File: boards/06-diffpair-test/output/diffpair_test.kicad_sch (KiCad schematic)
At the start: 7 parts, among them J1 USB-C, J3 MiniPCIe, J4 FFC4, U1 QFN32_USB2, U2 BGA49_USB3, U3 QFP48_PCIe, U4 QFN24_MIPI

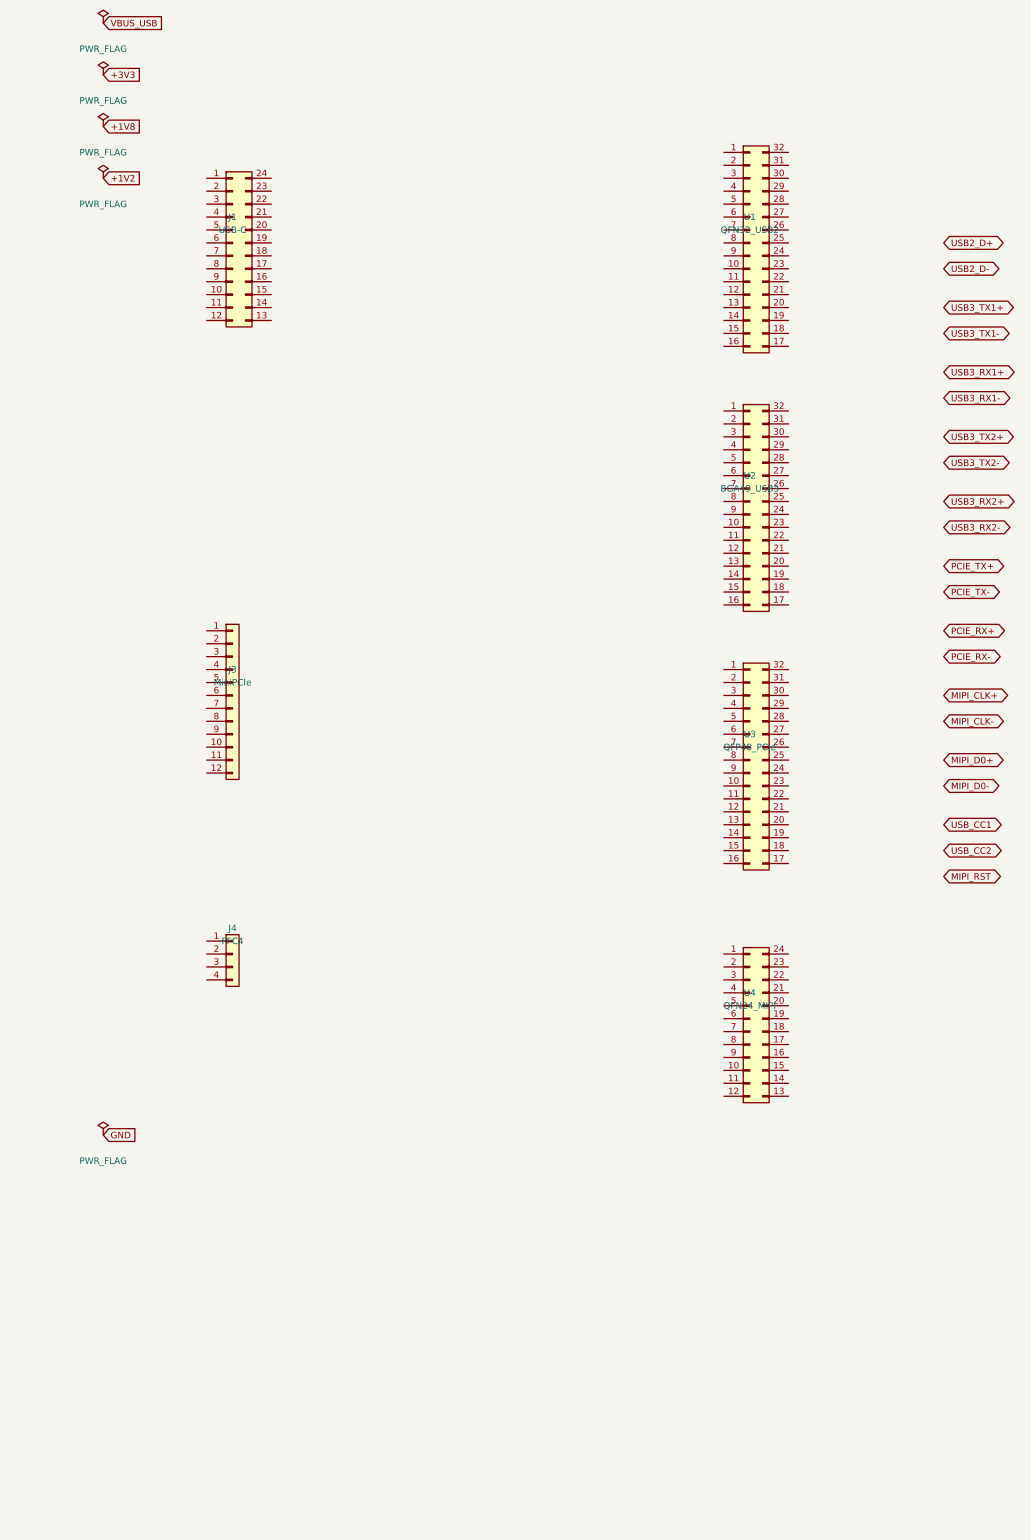
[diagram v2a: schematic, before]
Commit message: feat(lvs): wire boards 06/07 fixture schematics so LVS carries real evidence
Boards 06 (diffpair-test) and 07 (matchgroup-test) showed "LVS not run"
on the gallery because their PCB-first fixture schematics contained ZERO
(wire ...) elements: every pin floated, _schematic_pin_to_net bound 0
pins, and the #4011 vacuity guard correctly refused clean=true on zero
evidence.  This wires both schematics for real:

Schematic generators (the fix):
* Both generate_schematic.py scripts now synthesize one testbench symbol
  per component via kicad_tools.schematic.symbol_generator, with pin
  numbers matching the PCB pads EXACTLY (USB-C A1..B12+S1/S2, BGA A1..G7,
  FFC M1/M2/RST -- stock Conn_01xN symbols with numeric pins could never
  bind those pads), written to a project-local .kicad_sym and resolved
  via Schematic(local_symbol_libs=[...]) (the board-05 pattern).
* Every pin gets a wire stub (endpoint-attached, per KiCad semantics) +
  a global label naming its net; PIN_NETS mirrors generate_pcb.py
  pad-for-pad.  Bound pins: board 06 0/198 -> 198/198, board 07
  0/244 -> 244/244.

Verified LVS outcomes (committed artifacts):
* Board 06: copper 0 shorts / 0 opens on 198 bound pads AND label 0
  mismatches -> lvs.json clean=true; recipe now hard-gates on BOTH
  comparators (require_clean=True, boards 00-02 style).  board.json:
  status=ok, lvs_clean=true -> gallery Ready.
* Board 07: label clean, copper HONESTLY reports exactly the 5
  seed-invariant unroutable nets (#3438: DQ3, DQ4, MIPI_DAT0_N,
  TMDS_D0_N, TMDS_D1_N) as opens -> committed lvs.json clean=false with
  5 copper opens.  Recipe keeps require_clean=False (the opens are
  expected) with an accurate warning.  board.json: status=partial,
  lvs_clean=false, lvs_mismatches=5 -- the truthful state.

board-metrics:
* _parse_lvs now counts copper_mismatches in lvs_mismatches (label leg
  alone would render a dishonest "0 mismatches" for board 07's
  clean=false report).  All other committed boards have 0 copper
  mism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
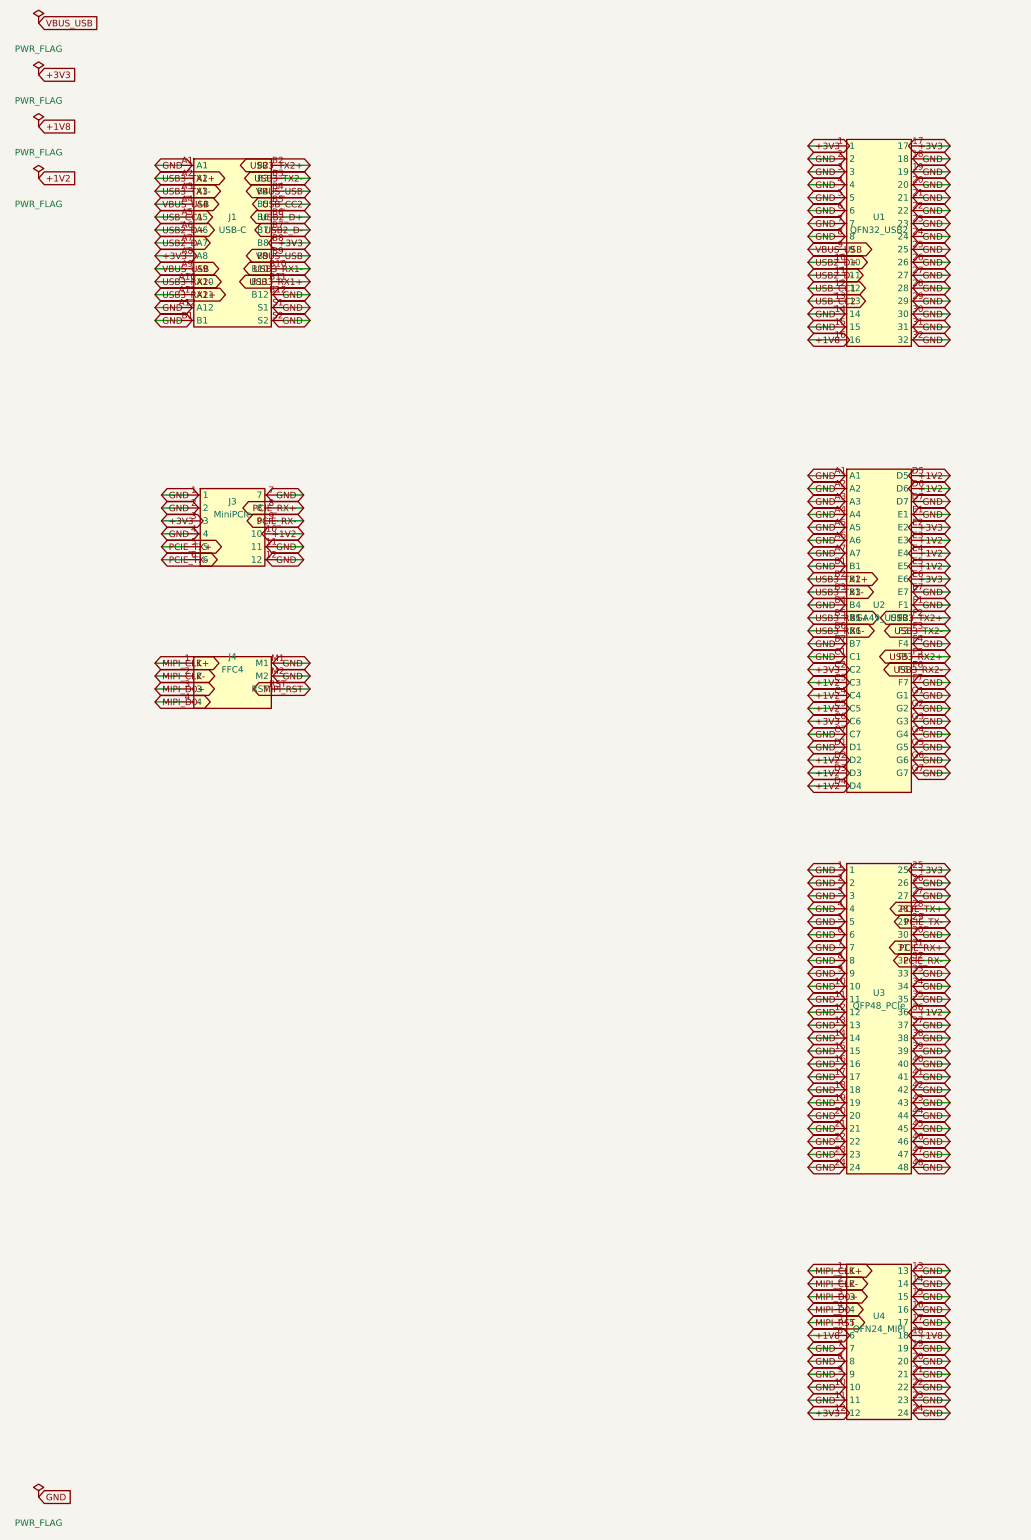
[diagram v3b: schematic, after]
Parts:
- removed J1: USB-C, Connector_USB:USB_C_Receptacle_USB2.0, symbol Connector_Generic:Conn_02x12_Counter_Clockwise
- removed J3: MiniPCIe, Connector_PCIE:PCIE_Mini_Edge, symbol Connector_Generic:Conn_01x12
- removed J4: FFC4, Connector_FFC:FFC_4P_0.5mm, symbol Connector_Generic:Conn_01x04
- removed U1: QFN32_USB2, Package_DFN_QFN:QFN-32-1EP_5x5mm_P0.5mm, symbol Connector_Generic:Conn_02x16_Counter_Clockwise
- removed U2: BGA49_USB3, Package_BGA:BGA-49_5.0x5.0mm_Layout7x7_P0.5mm, symbol Connector_Generic:Conn_02x16_Counter_Clockwise
- removed U3: QFP48_PCIe, Package_QFP:LQFP-48_7x7mm_P0.5mm, symbol Connector_Generic:Conn_02x16_Counter_Clockwise
- removed U4: QFN24_MIPI, Package_DFN_QFN:QFN-24-1EP_4x4mm_P0.5mm, symbol Connector_Generic:Conn_02x12_Counter_Clockwise
- added J1: USB-C, Connector_USB:USB_C_Receptacle_USB2.0, symbol diffpair_lvs:USBC_SRC
- added J3: MiniPCIe, Connector_PCIE:PCIE_Mini_Edge, symbol diffpair_lvs:MINIPCIE_SRC
- added J4: FFC4, Connector_FFC:FFC_4P_0.5mm, symbol diffpair_lvs:FFC_SRC
- added U1: QFN32_USB2, Package_DFN_QFN:QFN-32-1EP_5x5mm_P0.5mm, symbol diffpair_lvs:QFN32_USB2
- added U2: BGA49_USB3, Package_BGA:BGA-49_5.0x5.0mm_Layout7x7_P0.5mm, symbol diffpair_lvs:BGA49_USB3
- added U3: QFP48_PCIe, Package_QFP:LQFP-48_7x7mm_P0.5mm, symbol diffpair_lvs:QFP48_PCIE
- added U4: QFN24_MIPI, Package_DFN_QFN:QFN-24-1EP_4x4mm_P0.5mm, symbol diffpair_lvs:QFN24_MIPI
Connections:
- net +1V2: now also J3.10, U2.C3, U2.C4, U2.C5, U2.D2, U2.D3, U2.D4, U2.D5, U2.D6, U2.E3, U2.E4, U2.E5, U3.36
- net +1V8: now also U1.16, U4.18, U4.6
- net +3V3: now also J1.A8, J1.B8, J3.3, U1.1, U1.17, U2.C2, U2.C6, U2.E2, U2.E6, U3.25, U4.12
- net GND: now also J1.A1, J1.A12, J1.B1, J1.B12, J1.S1, J1.S2, J3.1, J3.11, J3.12, J3.2, J3.4, J3.7, J4.M1, J4.M2, U1.14, U1.15, U1.18, U1.19, U1.2, U1.20, U1.21, U1.22, U1.23, U1.24, U1.25, U1.26, U1.27, U1.28, U1.29, U1.3, U1.30, U1.31, U1.32, U1.4, U1.5, U1.6, U1.7, U1.8, U2.A1, U2.A2, U2.A3, U2.A4, U2.A5, U2.A6, U2.A7, U2.B1, U2.B4, U2.B7, U2.C1, U2.C7, U2.D1, U2.D7, U2.E1, U2.E7, U2.F1, U2.F4, U2.F7, U2.G1, U2.G2, U2.G3, U2.G4, U2.G5, U2.G6, U2.G7, U3.1, U3.10, U3.11, U3.12, U3.13, U3.14, U3.15, U3.16, U3.17, U3.18, U3.19, U3.2, U3.20, U3.21, U3.22, U3.23, U3.24, U3.26, U3.27, U3.3, U3.30, U3.33, U3.34, U3.35, U3.37, U3.38, U3.39, U3.4, U3.40, U3.41, U3.42, U3.43, U3.44, U3.45, U3.46, U3.47, U3.48, U3.5, U3.6, U3.7, U3.8, U3.9, U4.10, U4.11, U4.13, U4.14, U4.15, U4.16, U4.17, U4.19, U4.20, U4.21, U4.22, U4.23, U4.24, U4.7, U4.8, U4.9
- net MIPI_CLK+: now also J4.1, U4.1
- net MIPI_CLK-: now also J4.2, U4.2
- net MIPI_D0+: now also J4.3, U4.3
- net MIPI_D0-: now also J4.4, U4.4
- net MIPI_RST: now also J4.RST, U4.5
- net PCIE_RX+: now also J3.8, U3.31
- net PCIE_RX-: now also J3.9, U3.32
- net PCIE_TX+: now also J3.5, U3.28
- net PCIE_TX-: now also J3.6, U3.29
- net USB2_D+: now also J1.A6, J1.B6, U1.10
- net USB2_D-: now also J1.A7, J1.B7, U1.11
- net USB3_RX1+: now also J1.B11, U2.B5
- net USB3_RX1-: now also J1.B10, U2.B6
- net USB3_RX2+: now also J1.A11, U2.F5
- net USB3_RX2-: now also J1.A10, U2.F6
- net USB3_TX1+: now also J1.A2, U2.B2
- net USB3_TX1-: now also J1.A3, U2.B3
- net USB3_TX2+: now also J1.B2, U2.F2
- net USB3_TX2-: now also J1.B3, U2.F3
- net USB_CC1: now also J1.A5, U1.12
- net USB_CC2: now also J1.B5, U1.13
- net VBUS_USB: now also J1.A4, J1.A9, J1.B4, J1.B9, U1.9
